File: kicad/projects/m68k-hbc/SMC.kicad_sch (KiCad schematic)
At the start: 23 parts, among them J12 ICSP_SMC, J17 Conn_02x12_Odd_Even, U14 25LCxxx, U15 DS1307+, U17 PCA9306D, U18 SN74LV1T34DBV, U20 SN74LV1T34DBV, U21 SN74LV1T34DBV, U31 ATmegA32-16P, U35 Si5351A-B-GT, Y1 32.768k, Y2 16M, Y3 25M

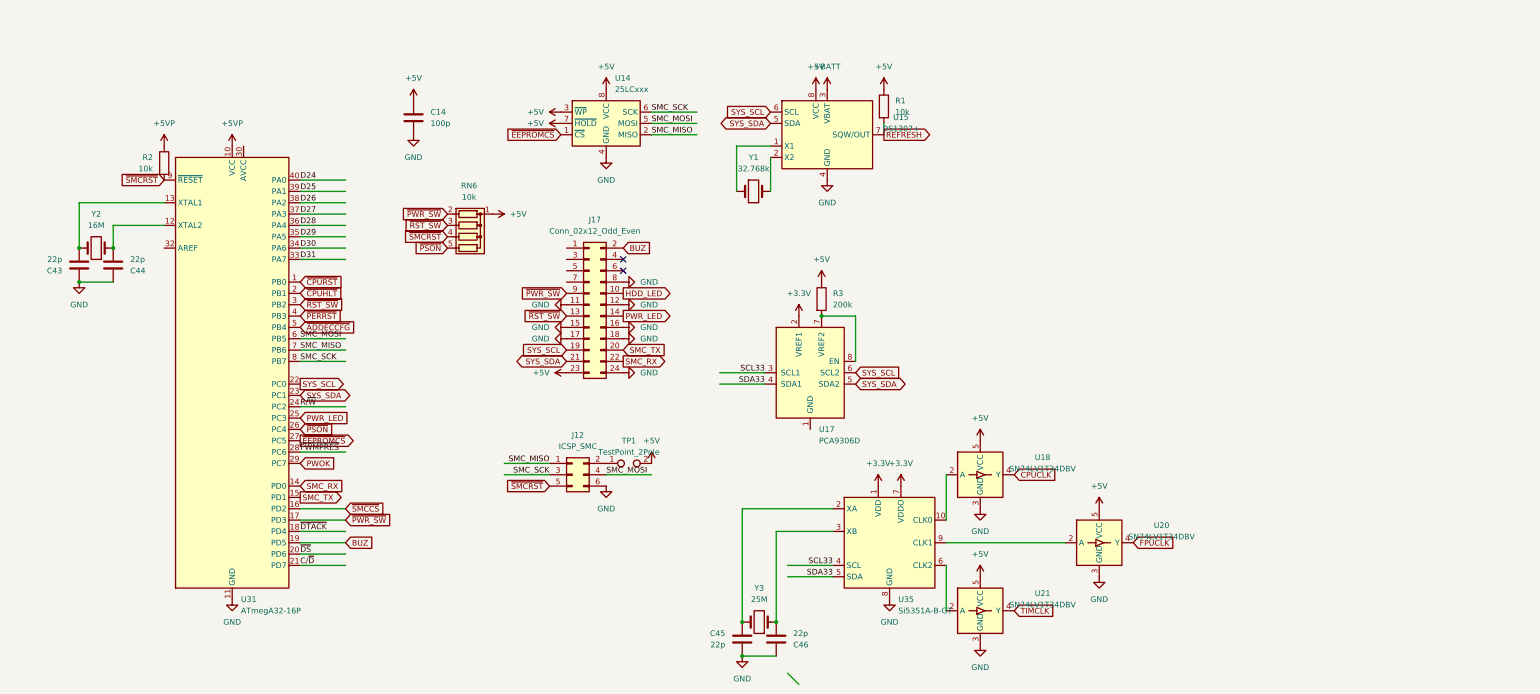
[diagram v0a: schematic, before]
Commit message: Modified system architecture, New KiCad Project: Cache Memory Module(SIMM80)
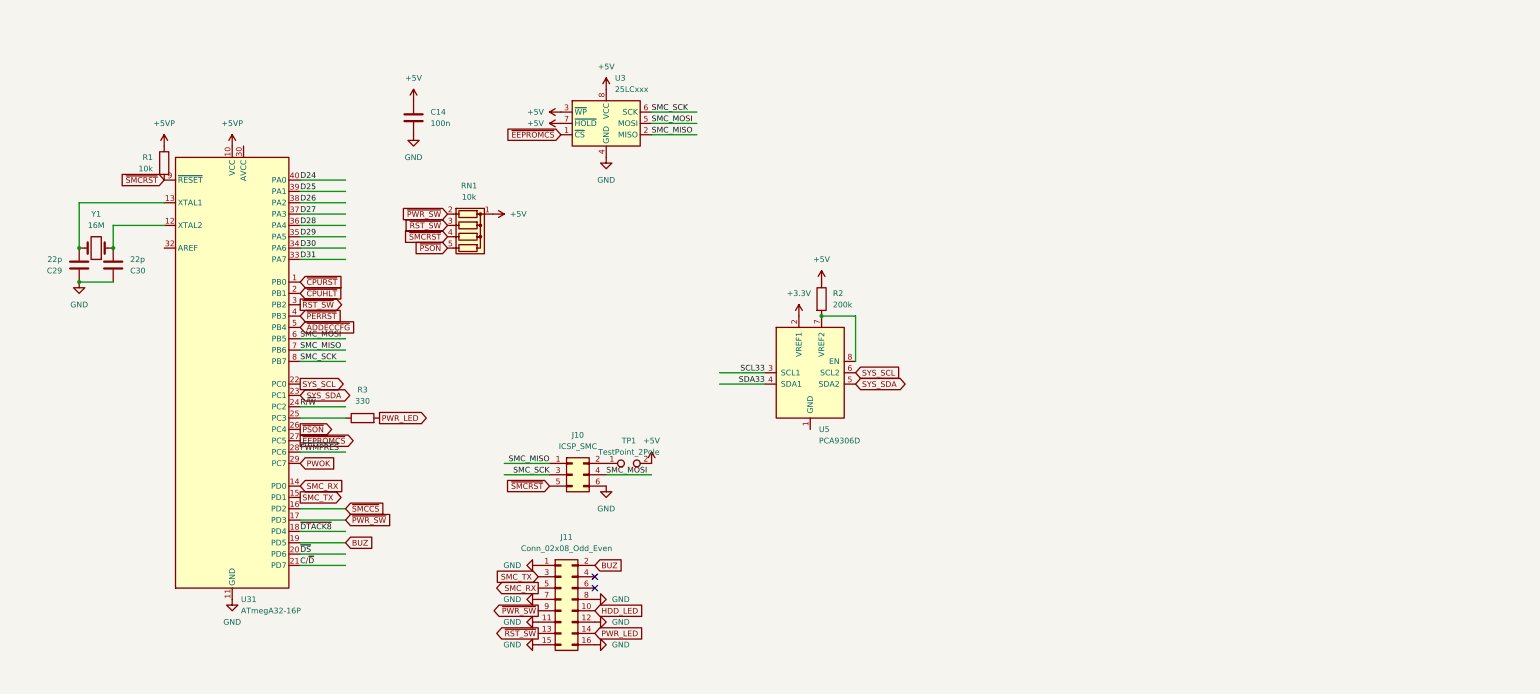
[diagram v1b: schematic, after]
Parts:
- removed C45, C46: 22p, Capacitor_SMD:C_1206_3216Metric_Pad1.33x1.80mm_HandSolder, symbol Device:C
- removed J17: Conn_02x12_Odd_Even, Connector_PinHeader_2.54mm:PinHeader_2x12_P2.54mm_Vertical, symbol Connector_Generic:Conn_02x12_Odd_Even
- removed R1: 10k, Resistor_SMD:R_1206_3216Metric_Pad1.30x1.75mm_HandSolder, symbol Device:R
- removed U15: DS1307+, Package_DIP:DIP-8_W7.62mm, symbol Timer_RTC:DS1307+
- removed U18, U20, U21: SN74LV1T34DBV, Package_TO_SOT_SMD:SOT-23-5, symbol Logic_LevelTranslator:SN74LV1T34DBV
- removed U35: Si5351A-B-GT, Package_SO:MSOP-10_3x3mm_P0.5mm, symbol Oscillator:Si5351A-B-GT
- removed Y1: 32.768k, Crystal:Crystal_Round_D2.0mm_Vertical, symbol Device:Crystal
- removed Y3: 25M, Crystal:Crystal_HC52-6mm_Vertical, symbol Device:Crystal
- added J11: Conn_02x08_Odd_Even, Connector_PinHeader_2.54mm:PinHeader_2x08_P2.54mm_Vertical, symbol Connector_Generic:Conn_02x08_Odd_Even
- added R3: 330, Resistor_SMD:R_1206_3216Metric_Pad1.30x1.75mm_HandSolder, symbol Device:R
- C14: value 100p -> 100n
- renumbered C43 to C29, C44 to C30, J12 to J10, R2 to R1, R3 to R2, RN6 to RN1, U14 to U3, U17 to U5, Y2 to Y1
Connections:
- net BUZ: now also J11.2 (Pin_2)
- net GND: now also J11.1 (Pin_1), J11.11 (Pin_11), J11.12 (Pin_12), J11.15 (Pin_15), J11.16 (Pin_16), J11.7 (Pin_7), J11.8 (Pin_8)
- net HDD_LED: now also J11.10 (Pin_10)
- net PWR_LED: now also J11.14 (Pin_14), R3.2; no longer U31.25 (PC3)
- net SMC_RX: now also J11.5 (Pin_5)
- net SMC_TX: now also J11.3 (Pin_3)
- net ~{PWR_SW}: now also J11.9 (Pin_9)
- net ~{RST_SW}: now also J11.13 (Pin_13)
- net ~{DTACK} renamed ~{DTACK8}
- new net: R3.1, U31.25 (PC3)

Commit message: Some Updates
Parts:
- removed C14: 100n, Capacitor_SMD:C_1206_3216Metric_Pad1.33x1.80mm_HandSolder, symbol Device:C
- removed J11: Conn_02x08_Odd_Even, Connector_PinHeader_2.54mm:PinHeader_2x08_P2.54mm_Vertical, symbol Connector_Generic:Conn_02x08_Odd_Even
- removed R2: 200k, Resistor_SMD:R_1206_3216Metric_Pad1.30x1.75mm_HandSolder, symbol Device:R
- removed R3: 330, Resistor_SMD:R_1206_3216Metric_Pad1.30x1.75mm_HandSolder, symbol Device:R
- removed RN1: 10k, Resistor_THT:R_Array_SIP5, symbol Device:R_Network04
- removed U3: 25LCxxx, Package_DIP:DIP-8_W7.62mm_Socket, symbol Memory_EEPROM:25LCxxx
- removed U5: PCA9306D, Package_SO:SO-8_3.9x4.9mm_P1.27mm, symbol Interface:PCA9306D
- added U39: SYS_Header, Connector_PinHeader_2.54mm:PinHeader_2x08_P2.54mm_Vertical, symbol m68k-hbc-conn:SYS_Header
- C55: renamed from C29; value 22p -> C; footprint Capacitor_SMD:C_1206_3216Metric_Pad1.33x1.80mm_HandSolder -> Capacitor_SMD:C_0603_1608Metric_Pad1.08x0.95mm_HandSolder
- C56: renamed from C30; value 22p -> C; footprint Capacitor_SMD:C_1206_3216Metric_Pad1.33x1.80mm_HandSolder -> Capacitor_SMD:C_0603_1608Metric_Pad1.08x0.95mm_HandSolder
- J10: value ICSP_SMC -> Conn_02x03_Odd_Even
- R2: renamed from R1; value 10k -> R; footprint Resistor_SMD:R_1206_3216Metric_Pad1.30x1.75mm_HandSolder -> Resistor_SMD:R_0603_1608Metric_Pad0.98x0.95mm_HandSolder
- U31: value ATmegA32-16P -> ATmega32-16P
- Y1: value 16M -> Crystal
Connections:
- net +5V: now also U39.4 (+5V)
- net +5VP: now also U39.8 (+5VSB)
- net BUZ: now also U39.1 (BUZ+)
- net GND: now also U39.11 (HDD-), U39.12 (RSW-), U39.15 (PWR-), U39.16 (PSW-), U39.2 (GND), U39.6 (GND), U39.7 (BUZ-)
- net SMC_MISO: now also U31.6 (PB5); no longer U31.7 (PB6)
- net SMC_MOSI: now also U31.7 (PB6); no longer U31.6 (PB5)
- net LED_PWR: now reaches U31.25 (PC3)
- net LED_PWR: now also U39.13 (PWR+)
- net C/~{D}: no longer names the net of U31.21 (PD7)
- net D24 renamed OPB_D0
- net D25 renamed OPB_D1
- net D26 renamed OPB_D2
- net D27 renamed OPB_D3
- net D28 renamed OPB_D4
- net D29 renamed OPB_D5
- net D30 renamed OPB_D6
- net D31 renamed OPB_D7
- net R/~{W} renamed OPB_R/~{W}
- net SYS_SCL renamed SMC_SCL
- net SYS_SDA renamed SMC_SDA
- net ~{ADDECCFG} renamed OPB_A3
- net ~{CPUHLT} renamed OPB_A1
- net ~{CPURST} renamed OPB_A0
- net ~{DS} renamed ~{OPB_DS}
- net ~{DTACK8} renamed ~{OPB_DTACK8}
- net ~{EEPROMCS}: no longer names the net of U31.27 (PC5)
- net ~{FWMPRES} renamed ~{IRQ_SMC}
- net ~{PERRST} renamed OPB_A2
- net ~{PWR_SW} renamed ~{SW_PWR}
- net ~{SW_PWR}: now also U39.14 (PSW+)
- net ~{RST_SW} renamed ~{SW_RST}
- net ~{SW_RST}: now also U39.10 (RSW+)
- net ~{SMCCS} renamed ~{CS_SMC}
- net ~{SMCRST} renamed ~{RST_SMC}
- new net LED_HDD: U39.9 (HDD+)
- no-connect marks 2 -> 0
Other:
- note added: "OPB Signals"

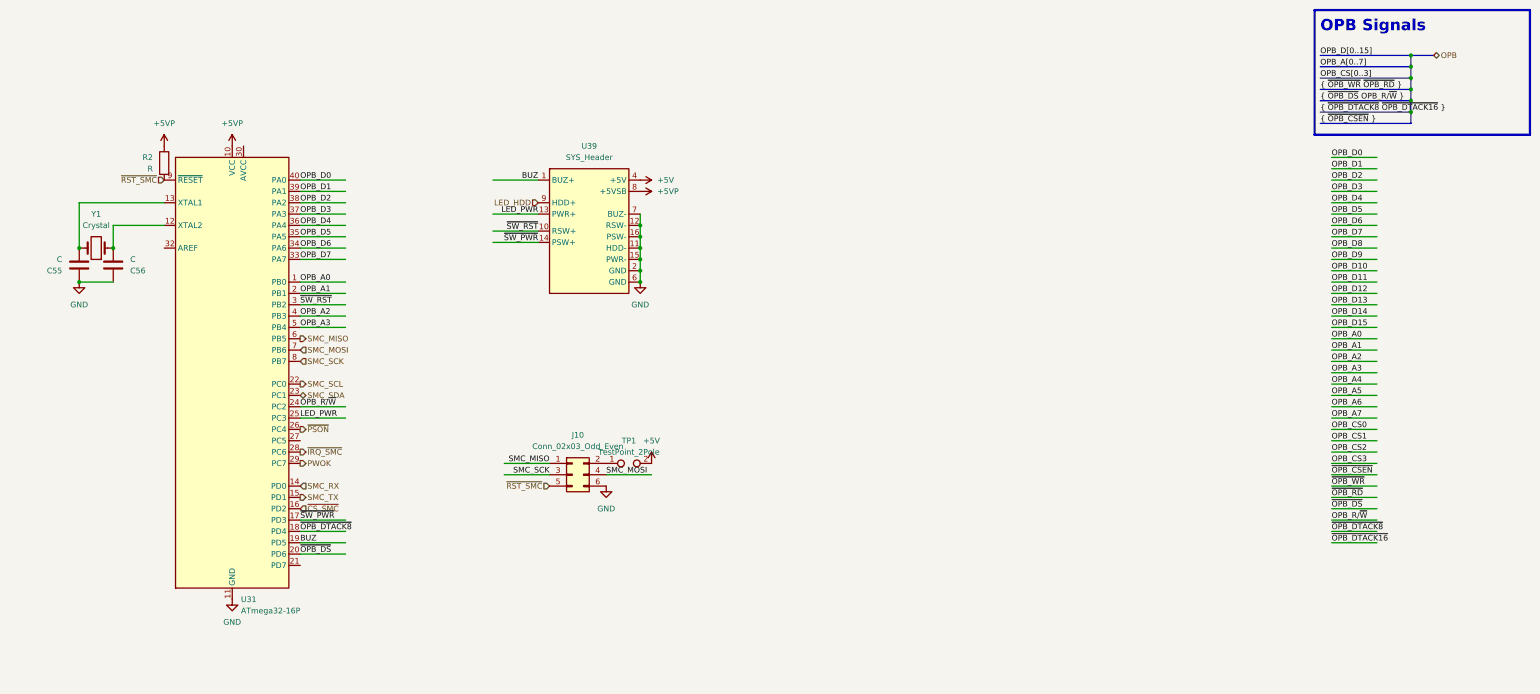
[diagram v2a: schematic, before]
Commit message: Large changes: EHBCSimpleEmu, kicad, fwcode, docs
This commit contains some large changes:
- Removed EHBCSimpleEmu (Moved to kms1212/llemu, kms1212/qemu)
- (likely) Removed fwcode; now it only boots and stops
- Modified documents
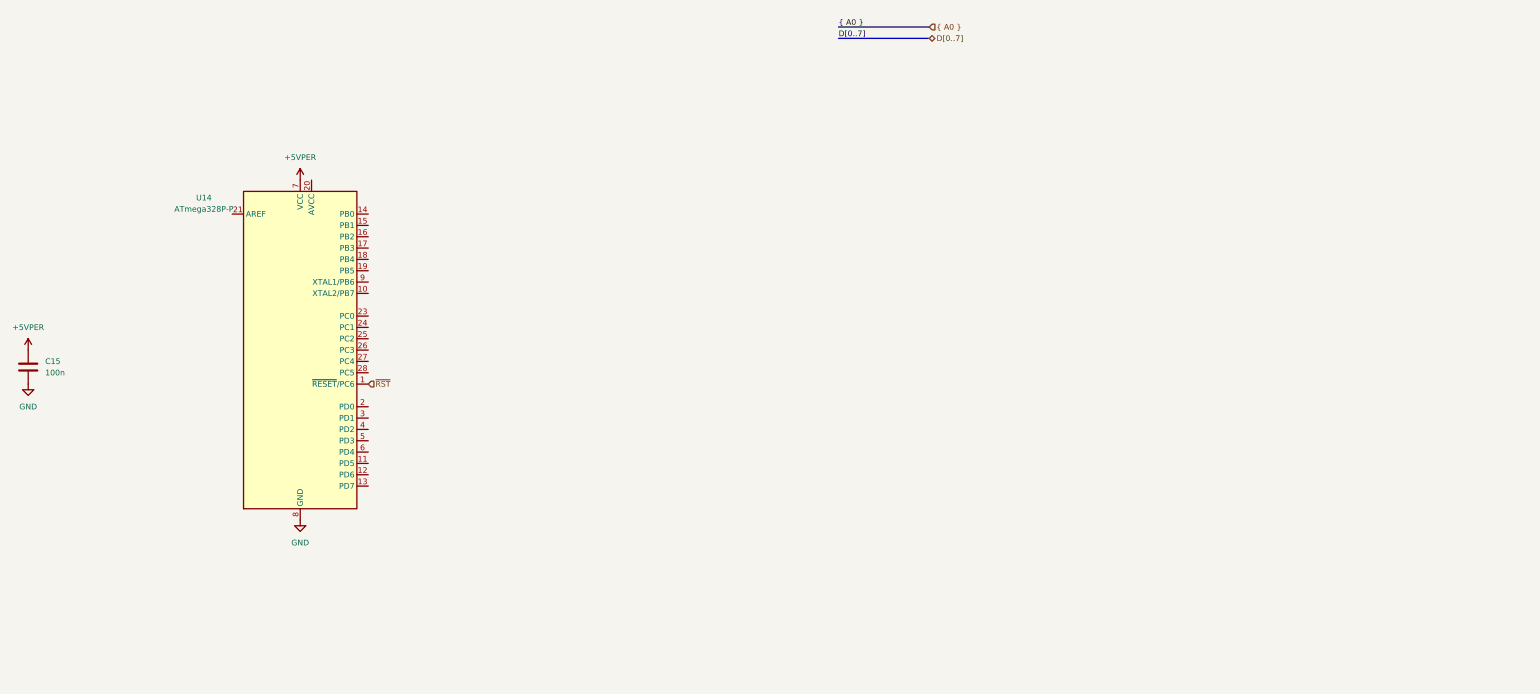
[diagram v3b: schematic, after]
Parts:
- removed C55, C56: C, Capacitor_SMD:C_0603_1608Metric_Pad1.08x0.95mm_HandSolder, symbol Device:C
- removed J10: Conn_02x03_Odd_Even, Connector_PinSocket_2.54mm:PinSocket_2x03_P2.54mm_Vertical, symbol Connector_Generic:Conn_02x03_Odd_Even
- removed R2: R, Resistor_SMD:R_0603_1608Metric_Pad0.98x0.95mm_HandSolder, symbol Device:R
- removed TP1: TestPoint_2Pole, Connector_PinHeader_1.00mm:PinHeader_1x02_P1.00mm_Vertical, symbol Connector:TestPoint_2Pole
- removed U31: ATmega32-16P, Package_DIP:DIP-40_W15.24mm, symbol MCU_Microchip_ATmega:ATmega32-16P
- removed U39: SYS_Header, Connector_PinHeader_2.54mm:PinHeader_2x08_P2.54mm_Vertical, symbol m68k-hbc-conn:SYS_Header
- removed Y1: Crystal, Crystal:Crystal_HC52-6mm_Vertical, symbol Device:Crystal
- added C15: 100n, Capacitor_THT:C_Disc_D6.0mm_W2.5mm_P5.00mm, symbol Device:C
- added U14: ATmega328P-P, Package_DIP:DIP-28_W7.62mm_Socket, symbol MCU_Microchip_ATmega:ATmega328P-P
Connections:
- net GND: now also C15.2, U14.22 (GND), U14.8 (GND)
- new net +5VPER: C15.1, U14.7 (VCC)
- new net ~{RST}: U14.1 (~{RESET}/PC6)
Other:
- note removed: "OPB Signals"
